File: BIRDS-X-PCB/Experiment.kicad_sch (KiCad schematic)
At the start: 19 parts, among them U301 VT01, U302 VT01, U303 VT01, U304 VT01, U305 TL974IPWR, U306 ADG734, U307 LM335DT, U308 LM334M

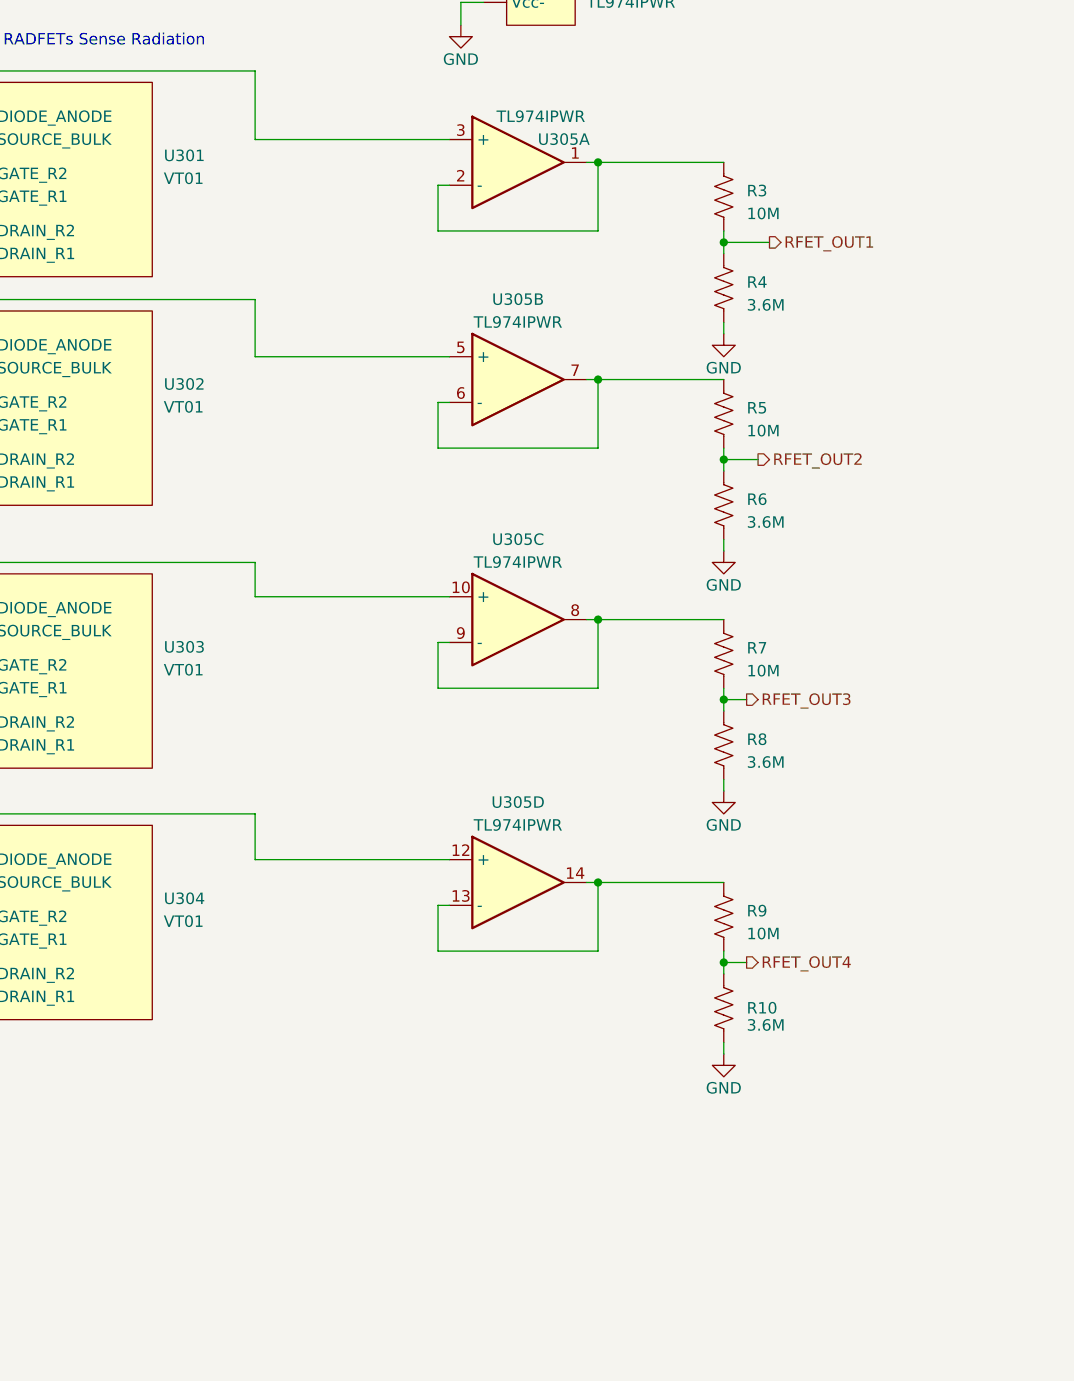
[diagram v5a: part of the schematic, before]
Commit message: Finish footprints assignment
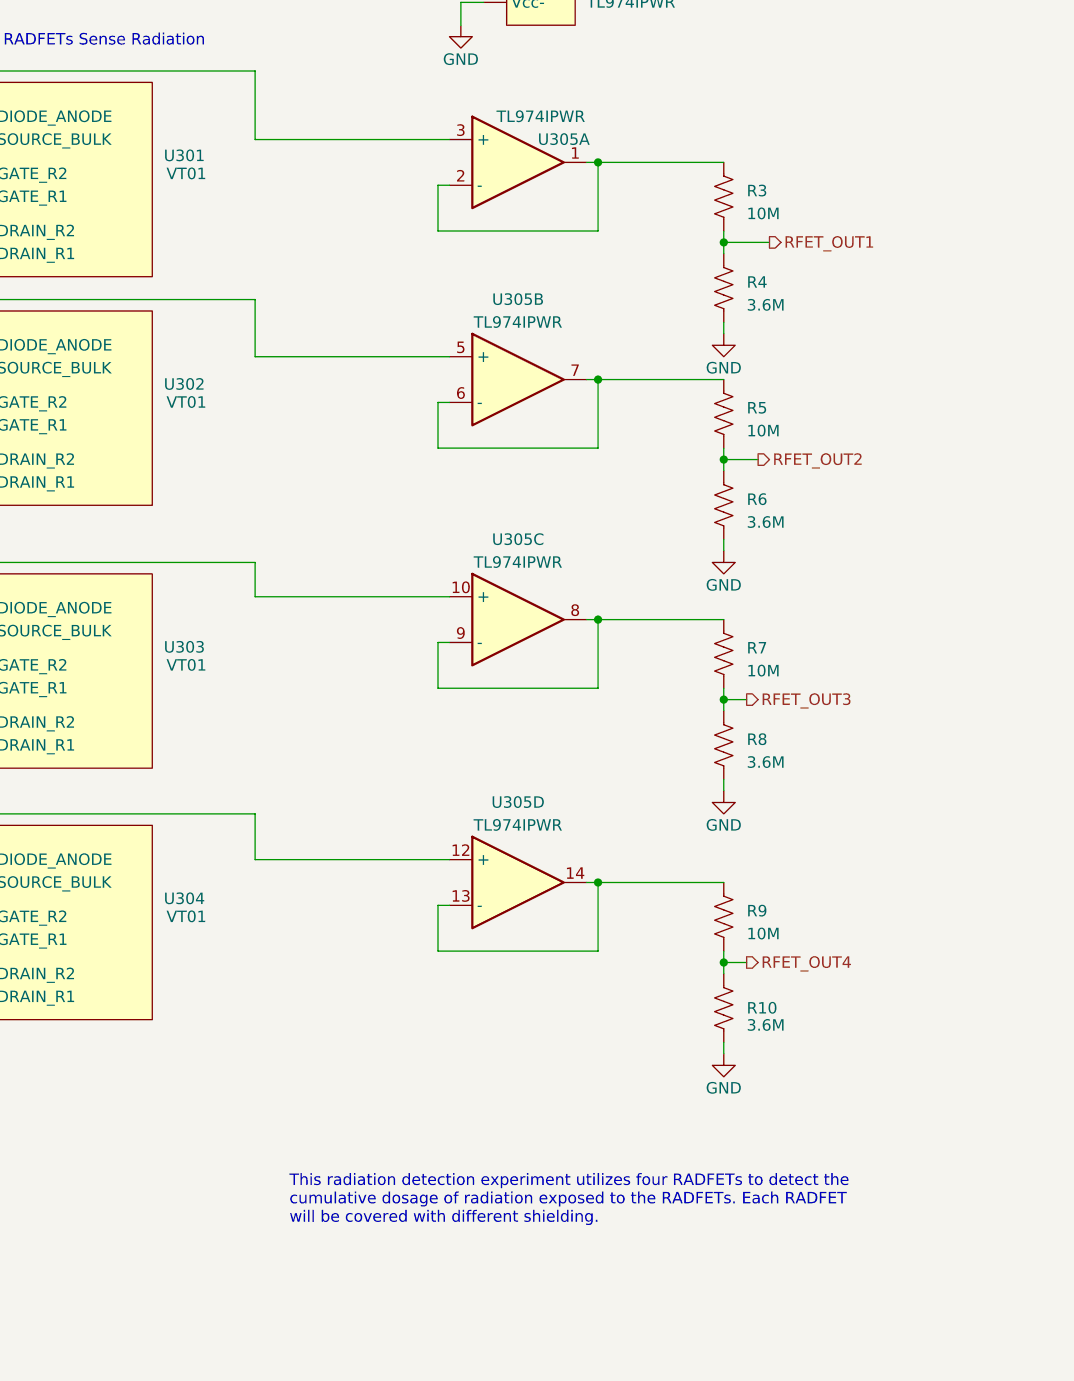
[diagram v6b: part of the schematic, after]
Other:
- note added: "This radiation detection experiment utilizes four RADFETs to detect the cumulative dosage of radiation exposed to the RADFETs. Each RADFET will be covered with different shielding."
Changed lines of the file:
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@@
+    (effects (font (size 1.27 1.27)) (justify left bottom))
+  )
+  (text "This radiation detection experiment utilizes four RADFETs to detect the\ncumulative dosage of radiation exposed to the RADFETs. Each RADFET \nwill be covered with different shielding."
+    (at 161.29 180.34 0)
     (effects (font (size 1.27 1.27)) (justify left bottom))
   )
@@
   )
   (symbol (lib_id "BIRDS-X_Symbols_Lib:VT01_Radfet") (at 137.16 85.09 0) (unit 1)
-    (in_bom yes) (on_board yes) (dnp no) (fields_autoplaced)
+    (in_bom yes) (on_board yes) (dnp no)
     (property "Reference" "U302" (at 147.32 86.8957 0)
       (effects (font (size 1.27 1.27)) (justify left))
     )
-    (property "Value" "VT01" (at 147.32 89.4357 0)
-      (effects (font (size 1.27 1.27)) (justify left))
+    (property "Value" "VT01" (at 149.86 88.9 0)
+      (effects (font (size 1.27 1.27)))
     )
     (property "Footprint" "" (at 137.16 85.09 0)
@@
   )
   (symbol (lib_id "BIRDS-X_Symbols_Lib:VT01_Radfet") (at 137.16 142.24 0) (unit 1)
-    (in_bom yes) (on_board yes) (dnp no) (fields_autoplaced)
+    (in_bom yes) (on_board yes) (dnp no)
     (property "Reference" "U304" (at 147.32 144.0457 0)
       (effects (font (size 1.27 1.27)) (justify left))
     )
-    (property "Value" "VT01" (at 147.32 146.5857 0)
-      (effects (font (size 1.27 1.27)) (justify left))
+    (property "Value" "VT01" (at 149.86 146.05 0)
+      (effects (font (size 1.27 1.27)))
     )
     (property "Footprint" "" (at 137.16 142.24 0)
@@
   )
   (symbol (lib_id "BIRDS-X_Symbols_Lib:VT01_Radfet") (at 137.16 114.3 0) (unit 1)
-    (in_bom yes) (on_board yes) (dnp no) (fields_autoplaced)
+    (in_bom yes) (on_board yes) (dnp no)
     (property "Reference" "U303" (at 147.32 116.1057 0)
       (effects (font (size 1.27 1.27)) (justify left))
     )
-    (property "Value" "VT01" (at 147.32 118.6457 0)
-      (effects (font (size 1.27 1.27)) (justify left))
+    (property "Value" "VT01" (at 149.86 118.11 0)
+      (effects (font (size 1.27 1.27)))
     )
     (property "Footprint" "" (at 137.16 114.3 0)
@@
   )
   (symbol (lib_id "BIRDS-X_Symbols_Lib:VT01_Radfet") (at 137.16 59.69 0) (unit 1)
-    (in_bom yes) (on_board yes) (dnp no) (fields_autoplaced)
+    (in_bom yes) (on_board yes) (dnp no)
     (property "Reference" "U301" (at 147.32 61.4957 0)
       (effects (font (size 1.27 1.27)) (justify left))
     )
-    (property "Value" "VT01" (at 147.32 64.0357 0)
-      (effects (font (size 1.27 1.27)) (justify left))
+    (property "Value" "VT01" (at 149.86 63.5 0)
+      (effects (font (size 1.27 1.27)))
     )
     (property "Footprint" "" (at 137.16 59.69 0)

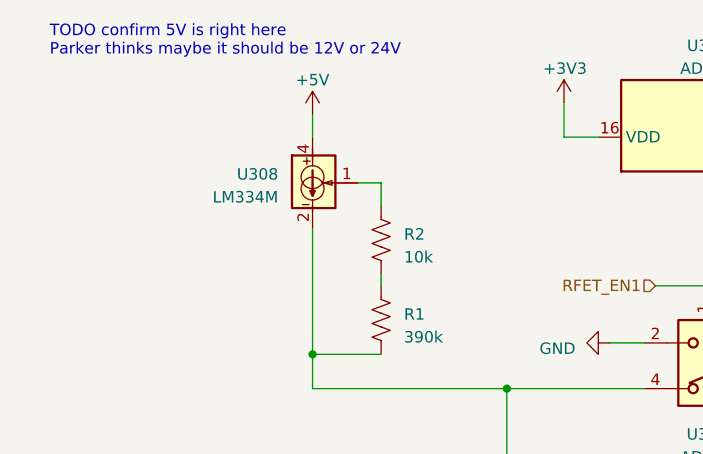
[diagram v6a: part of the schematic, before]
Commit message: Add core restricted layouts and lock them
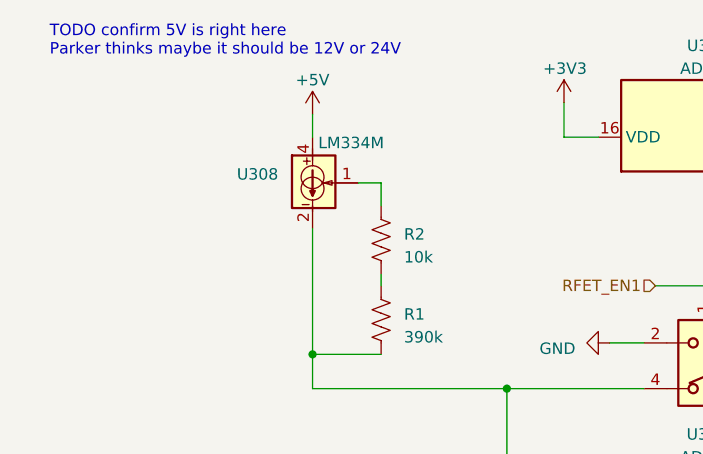
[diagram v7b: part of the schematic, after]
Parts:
- U301, U302, U303, U304: footprint (none) -> Package_SO:SO-6_4.4x3.6mm_P1.27mm
- U308: symbol Reference_Current:LM334M -> BIRDS-X_Symbols_Lib:LM334M
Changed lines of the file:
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@@
       (effects (font (size 1.27 1.27)))
     )
-    (property "Footprint" "" (at 137.16 85.09 0)
+    (property "Footprint" "Package_SO:SO-6_4.4x3.6mm_P1.27mm" (at 137.16 85.09 0)
       (effects (font (size 1.27 1.27)) hide)
     )
@@
     )
   )
-  (symbol (lib_id "Reference_Current:LM334M") (at 54.61 36.83 0) (unit 1)
+  (symbol (lib_id "BIRDS-X_Symbols_Lib:LM334M") (at 54.61 36.83 0) (unit 1)
     (in_bom yes) (on_board yes) (dnp no) (fields_autoplaced)
     (property "Reference" "U308" (at 50.8 35.8775 0)
       (effects (font (size 1.27 1.27)) (justify right))
     )
-    (property "Value" "LM334M" (at 50.8 38.4175 0)
-      (effects (font (size 1.27 1.27)) (justify right))
+    (property "Value" "LM334M" (at 55.245 32.385 0)
+      (effects (font (size 1.27 1.27)) (justify left))
     )
     (property "Footprint" "Package_SO:SOIC-8_3.9x4.9mm_P1.27mm" (at 55.245 40.64 0)
@@
     (pin "3")
     (pin "4")
+    (pin "5")
     (pin "6")
     (pin "7")
+    (pin "8")
     (instances
       (project "BIRDS-X-PCB"
@@
       (effects (font (size 1.27 1.27)))
     )
-    (property "Footprint" "" (at 137.16 142.24 0)
+    (property "Footprint" "Package_SO:SO-6_4.4x3.6mm_P1.27mm" (at 137.16 142.24 0)
       (effects (font (size 1.27 1.27)) hide)
     )
@@
       (effects (font (size 1.27 1.27)))
     )
-    (property "Footprint" "" (at 137.16 114.3 0)
+    (property "Footprint" "Package_SO:SO-6_4.4x3.6mm_P1.27mm" (at 137.16 114.3 0)
       (effects (font (size 1.27 1.27)) hide)
     )
@@
       (effects (font (size 1.27 1.27)))
     )
-    (property "Footprint" "" (at 137.16 59.69 0)
-      (effects (font (size 1.27 1.27)) hide)
-    )
+    (property "Footprint" "Package_SO:SO-6_4.4x3.6mm_P1.27mm" (at 137.16 59.69 0)
+      (effects (font (size 1.27 1.27)) hide)
+    )

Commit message: Add notes from schematic review session
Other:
- note added: "TODO add diode for temperature correction, and check new resistor calcs."
- note added: "TODO confirm if a single current source is adequate (maybe it should be 4x, if we want to measure them simultaneously)"
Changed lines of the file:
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@@
+    (effects (font (size 1.27 1.27)) (justify left bottom))
+  )
+  (text "TODO add diode for temperature correction,\nand check new resistor calcs."
+    (at 29.21 74.93 0)
     (effects (font (size 1.27 1.27)) (justify left bottom))
   )
@@
     (effects (font (size 1.27 1.27)) (justify left bottom))
   )
+  (text "TODO confirm if a single current\nsource is adequate (maybe it should be 4x,\nif we want to measure them simultaneously)"
+    (at 29.21 67.31 0)
+    (effects (font (size 1.27 1.27)) (justify left bottom))
+  )
